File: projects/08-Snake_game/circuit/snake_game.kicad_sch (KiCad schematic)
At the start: 11 parts, among them U1 1088B8, U2 74HC595

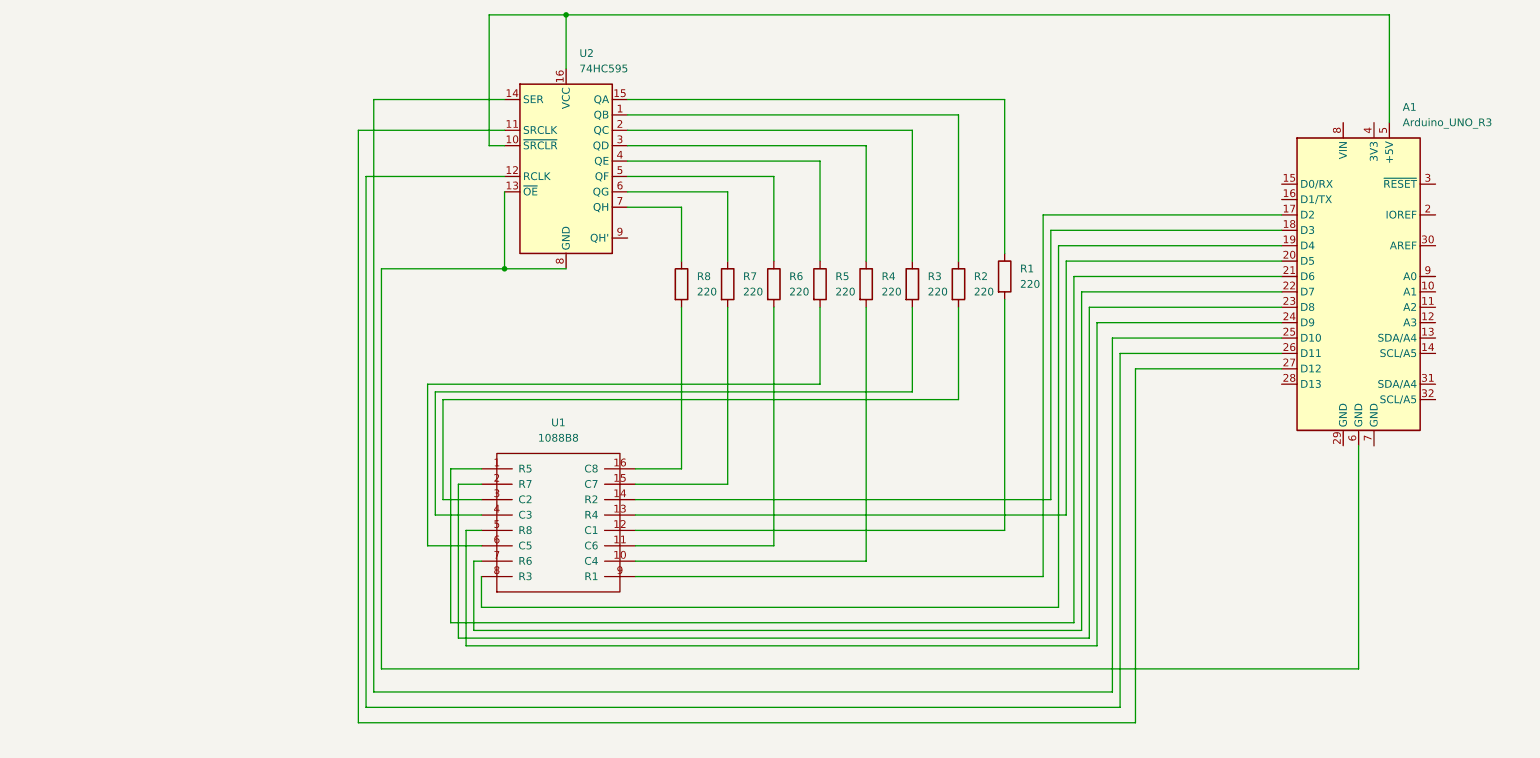
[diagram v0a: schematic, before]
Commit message: FEAT add the buttons to the circuit schemma
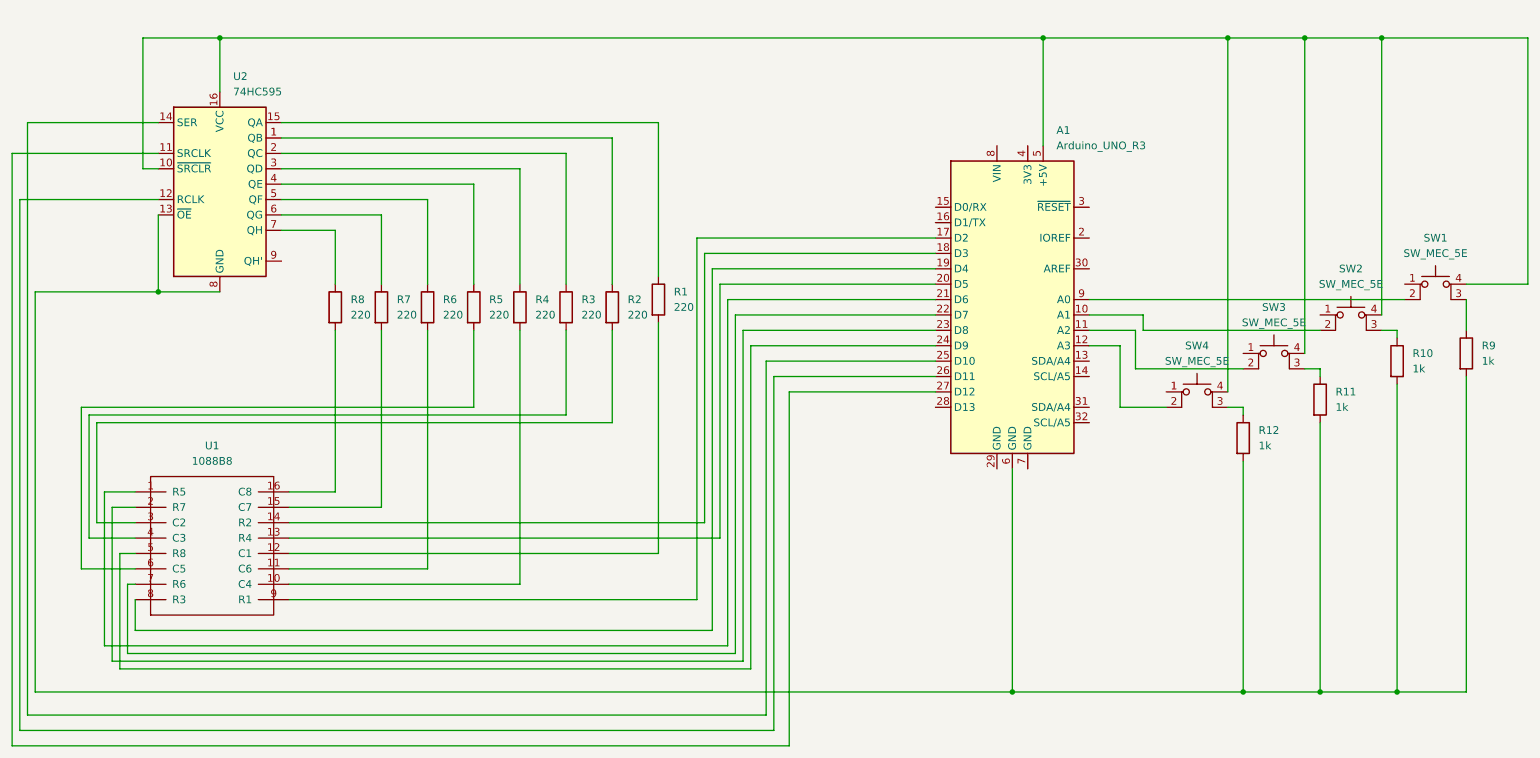
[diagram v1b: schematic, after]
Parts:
- added R10, R11, R12, R9: 1k, symbol Device:R
- added SW1, SW2, SW3, SW4: SW_MEC_5E, symbol Switch:SW_MEC_5E
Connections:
- net at A1.5 (+5V), U2.10 (~{SRCLR}), U2.16 (VCC): now also SW1.4 (A), SW2.4 (A), SW3.4 (A), SW4.4 (A)
- net at A1.6 (GND), U2.13 (~{OE}), U2.8 (GND): now also R10.2, R11.2, R12.2, R9.2
- net at A1.10 (A1): now also SW2.2
- net at A1.11 (A2): now also SW3.2
- net at A1.12 (A3): now also SW4.2
- net at A1.9 (A0): now also SW1.2
- new net: R11.1, SW3.3 (K)
- new net: R9.1, SW1.3 (K)
- new net: R10.1, SW2.3 (K)
- new net: R12.1, SW4.3 (K)
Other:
- moved on the sheet: A1, R1, R2, R3, R4, R5, R6, R7, R8, U1, U2
